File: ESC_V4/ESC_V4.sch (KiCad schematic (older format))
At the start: 43 parts

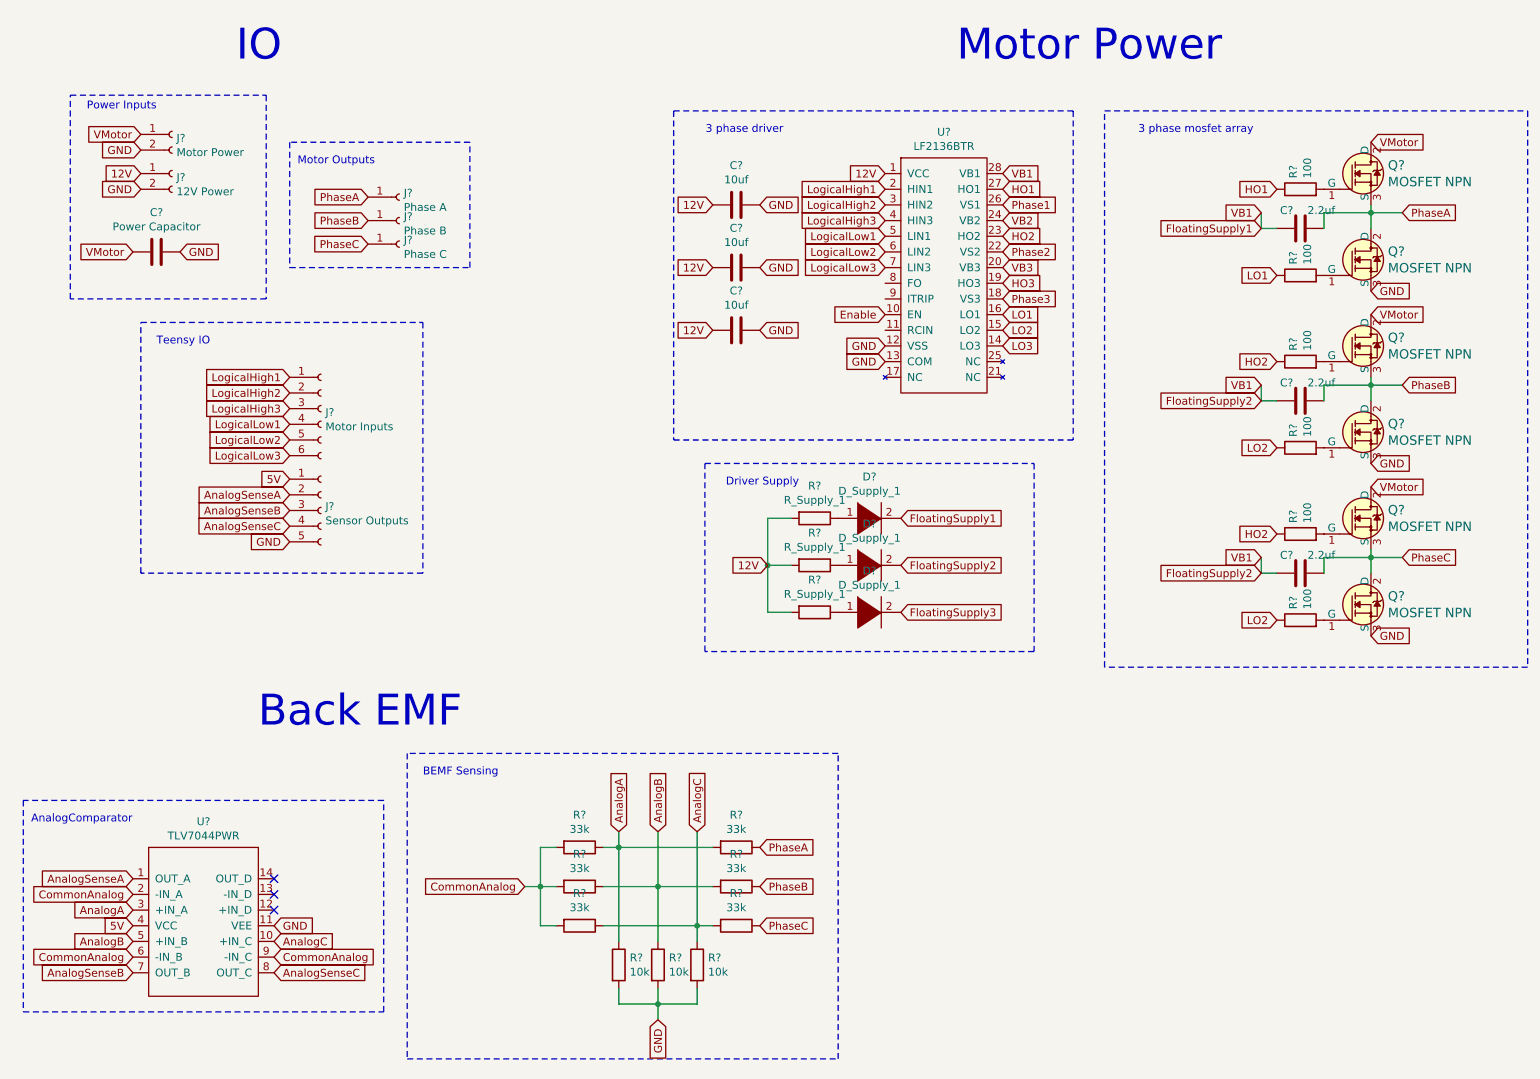
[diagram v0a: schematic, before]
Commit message: Footprint associations
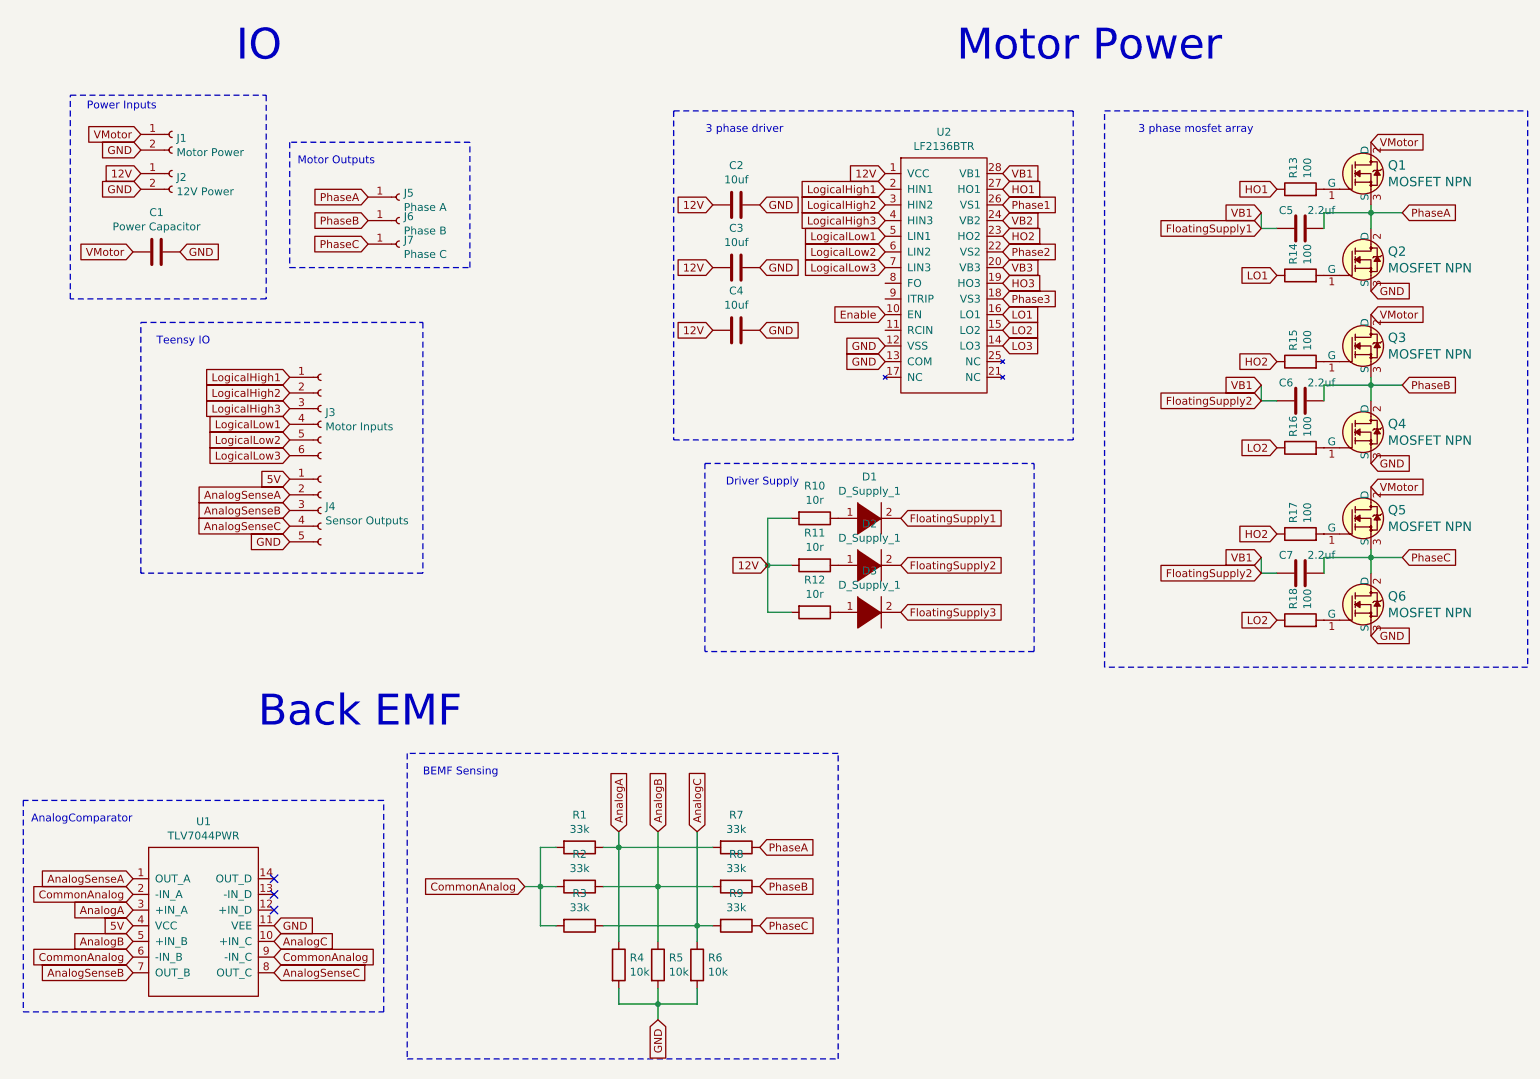
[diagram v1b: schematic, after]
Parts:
- C1: renamed from C?; footprint (none) -> Capacitor_SMD:C_Elec_10x10.2
- C2, C3, C4, C5, C6, C7: renamed from C?; footprint (none) -> Capacitor_SMD:C_0603_1608Metric
- D1, D2, D3: renamed from D?; footprint (none) -> Diode_SMD:D_SOD-323F
- J1: renamed from J?; footprint (none) -> XT60-M:AMASS_XT60-M
- J2: renamed from J?; footprint (none) -> Connector_PinHeader_2.54mm:PinHeader_1x02_P2.54mm_Vertical
- J3: renamed from J?; footprint (none) -> Connector_PinHeader_2.54mm:PinHeader_1x06_P2.54mm_Vertical
- J4: renamed from J?; footprint (none) -> Connector_PinHeader_2.54mm:PinHeader_1x05_P2.54mm_Vertical
- J5, J6, J7: renamed from J?; footprint (none) -> XT60-M:SquarePad4x4
- Q1, Q2, Q3, Q4, Q5: renamed from Q?; footprint digikey-footprints:TO-220-3 -> Package_TO_SOT_SMD:TO-252-2
- R1, R2, R3, R4: renamed from R?; footprint (none) -> Resistor_SMD:R_0603_1608Metric
- R10, R11, R12: renamed from R?; value R_Supply_1 -> 10r; footprint (none) -> Resistor_SMD:R_0201_0603Metric
- R13, R14, R15, R16, R17, R18, R5, R6, R7, R8, R9: renamed from R?; footprint (none) -> Resistor_SMD:R_0201_0603Metric
- U1: renamed from U?; footprint (none) -> Package_SO:TSSOP-14_4.4x5mm_P0.65mm
- U2: renamed from U?; footprint (none) -> Package_SO:SOIC-28W_7.5x17.9mm_P1.27mm
- gave numbers to parts that had none: 1

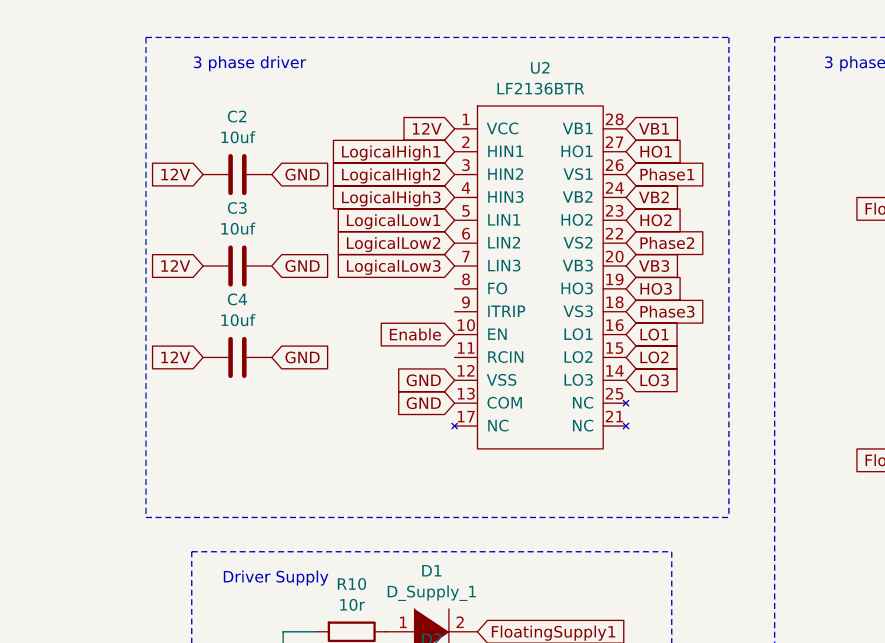
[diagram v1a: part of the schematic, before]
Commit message: Add components to driver and small tweaks
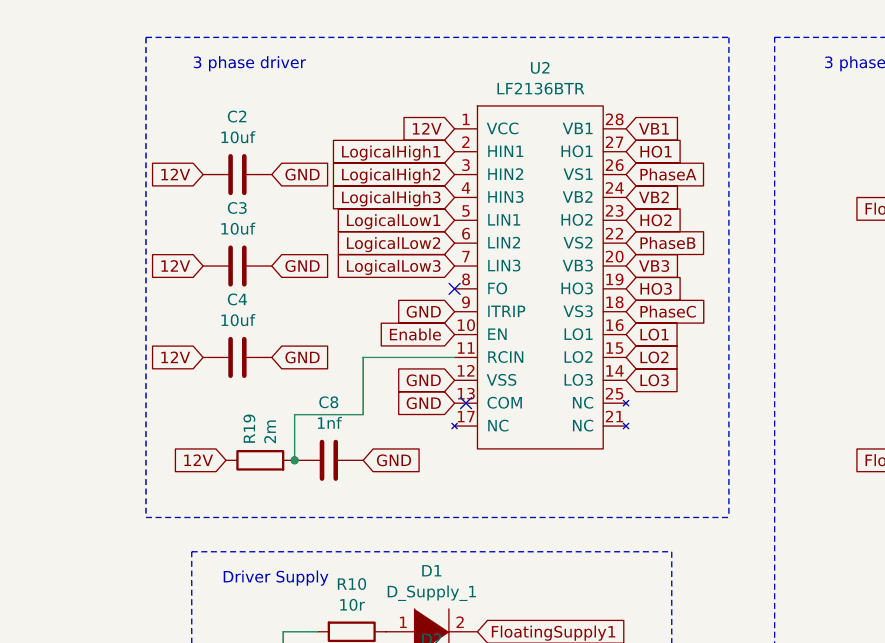
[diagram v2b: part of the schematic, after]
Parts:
- added C8: 1nf, Capacitor_SMD:C_0603_1608Metric, symbol Device:C
- added R19: 2m, Resistor_SMD:R_0201_0603Metric, symbol Device:R
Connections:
- net Phase1 is gone; now on net PhaseA: U2.26 (VS1)
- net Phase2 is gone; now on net PhaseB: U2.22 (VS2)
- net Phase3 is gone; now on net PhaseC: U2.18 (VS3)
- net 12V: now also R19.1
- net GND: now also U2.9 (ITRIP), C8.2
- net at U2.11 (RCIN): now also C8.1, R19.2
- no-connect marks 3 -> 5
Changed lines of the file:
@@
 LogicalLow3
 Text GLabel 7400 1900 2    50   Input ~ 0
-Phase1
+PhaseA
 Text GLabel 7400 2200 2    50   Input ~ 0
-Phase2
+PhaseB
 Text GLabel 7400 2500 2    50   Input ~ 0
-Phase3
+PhaseC
 Text GLabel 7400 1700 2    50   Input ~ 0
 VB1
@@
 	0    1    1    0
 $EndComp
+Text GLabel 6650 2500 0    50   Input ~ 0
+GND
+NoConn ~ 6650 2400
+NoConn ~ 6700 2900
+Wire Wire Line
+	6650 2700 6250 2700
+Wire Wire Line
+	5950 2950 5950 3150
+$Comp
+L Device:R R19
+U 1 1 623C84D3
+P 5800 3150
+F 0 "R19" H 5870 3196 50  0000 L CNN
+F 1 "2m" H 5870 3105 50  0000 L CNN
+F 2 "Resistor_SMD:R_0201_0603Metric" V 5730 3150 50  0001 C CNN
+F 3 "~" H 5800 3150 50  0001 C CNN
+	1    5800 3150
+	0    -1   -1   0
+$EndComp
+$Comp
+L Device:C C8
+U 1 1 623C9190
+P 6100 3150
+F 0 "C8" V 6352 3150 50  0000 C CNN
+F 1 "1nf" V 6261 3150 50  0000 C CNN
+F 2 "Capacitor_SMD:C_0603_1608Metric" H 6138 3000 50  0001 C CNN
+F 3 "~" H 6100 3150 50  0001 C CNN
+	1    6100 3150
+	0    -1   -1   0
+$EndComp
+Connection ~ 5950 3150
+Text GLabel 5650 3150 0    50   Input ~ 0
+12V
+Text GLabel 6250 3150 2    50   Input ~ 0
+GND
+Wire Wire Line
+	5950 2950 6250 2950
+Wire Wire Line
+	6250 2950 6250 2700
 $EndSCHEMATC

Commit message: Start of pcb layout
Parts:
- Q6: footprint digikey-footprints:TO-220-3 -> Package_TO_SOT_SMD:TO-252-2
- R10, R11, R12, R13, R14, R15, R16, R17, R18, R19, R5, R6, R7, R8, R9: footprint Resistor_SMD:R_0201_0603Metric -> Resistor_SMD:R_0603_1608Metric
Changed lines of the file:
@@
 F 0 "R7" V 5493 6000 50  0000 C CNN
 F 1 "33k" V 5584 6000 50  0000 C CNN
-F 2 "Resistor_SMD:R_0201_0603Metric" V 5630 6000 50  0001 C CNN
+F 2 "Resistor_SMD:R_0603_1608Metric" V 5630 6000 50  0001 C CNN
 F 3 "~" H 5700 6000 50  0001 C CNN
 	1    5700 6000
@@
 F 0 "R8" V 5493 6250 50  0000 C CNN
 F 1 "33k" V 5584 6250 50  0000 C CNN
-F 2 "Resistor_SMD:R_0201_0603Metric" V 5630 6250 50  0001 C CNN
+F 2 "Resistor_SMD:R_0603_1608Metric" V 5630 6250 50  0001 C CNN
 F 3 "~" H 5700 6250 50  0001 C CNN
 	1    5700 6250
@@
 F 0 "R9" V 5493 6500 50  0000 C CNN
 F 1 "33k" V 5584 6500 50  0000 C CNN
-F 2 "Resistor_SMD:R_0201_0603Metric" V 5630 6500 50  0001 C CNN
+F 2 "Resistor_SMD:R_0603_1608Metric" V 5630 6500 50  0001 C CNN
 F 3 "~" H 5700 6500 50  0001 C CNN
 	1    5700 6500
@@
 F 0 "R5" H 5270 6796 50  0000 L CNN
 F 1 "10k" H 5270 6705 50  0000 L CNN
-F 2 "Resistor_SMD:R_0201_0603Metric" V 5130 6750 50  0001 C CNN
+F 2 "Resistor_SMD:R_0603_1608Metric" V 5130 6750 50  0001 C CNN
 F 3 "~" H 5200 6750 50  0001 C CNN
 	1    5200 6750
@@
 F 0 "R6" H 5520 6796 50  0000 L CNN
 F 1 "10k" H 5520 6705 50  0000 L CNN
-F 2 "Resistor_SMD:R_0201_0603Metric" V 5380 6750 50  0001 C CNN
+F 2 "Resistor_SMD:R_0603_1608Metric" V 5380 6750 50  0001 C CNN
 F 3 "~" H 5450 6750 50  0001 C CNN
 	1    5450 6750
@@
 F 0 "Q6" H 9858 4503 60  0000 L CNN
 F 1 "MOSFET NPN" H 9858 4397 60  0000 L CNN
-F 2 "digikey-footprints:TO-220-3" H 9950 4650 60  0001 L CNN
+F 2 "Package_TO_SOT_SMD:TO-252-2" H 9950 4650 60  0001 L CNN
 F 3 "https://www.infineon.com/dgdl/irlb8721pbf.pdf?fileId=5546d462533600a40153566056732591" H 9950 4750 60  0001 L CNN
 F 4 "IRLB8721PBF-ND" H 9950 4850 60  0001 L CNN "Digi-Key_PN"
@@
 F 0 "R18" H 9370 4596 50  0000 L CNN
 F 1 "100" H 9370 4505 50  0000 L CNN
-F 2 "Resistor_SMD:R_0201_0603Metric" V 9230 4550 50  0001 C CNN
+F 2 "Resistor_SMD:R_0603_1608Metric" V 9230 4550 50  0001 C CNN
 F 3 "~" H 9300 4550 50  0001 C CNN
 	1    9300 4550
@@
 F 0 "R17" H 9370 4046 50  0000 L CNN
 F 1 "100" H 9370 3955 50  0000 L CNN
-F 2 "Resistor_SMD:R_0201_0603Metric" V 9230 4000 50  0001 C CNN
+F 2 "Resistor_SMD:R_0603_1608Metric" V 9230 4000 50  0001 C CNN
 F 3 "~" H 9300 4000 50  0001 C CNN
 	1    9300 4000
@@
 F 0 "R16" H 9370 3496 50  0000 L CNN
 F 1 "100" H 9370 3405 50  0000 L CNN
-F 2 "Resistor_SMD:R_0201_0603Metric" V 9230 3450 50  0001 C CNN
+F 2 "Resistor_SMD:R_0603_1608Metric" V 9230 3450 50  0001 C CNN
 F 3 "~" H 9300 3450 50  0001 C CNN
 	1    9300 3450
@@
 F 0 "R15" H 9370 2946 50  0000 L CNN
 F 1 "100" H 9370 2855 50  0000 L CNN
-F 2 "Resistor_SMD:R_0201_0603Metric" V 9230 2900 50  0001 C CNN
+F 2 "Resistor_SMD:R_0603_1608Metric" V 9230 2900 50  0001 C CNN
 F 3 "~" H 9300 2900 50  0001 C CNN
 	1    9300 2900
@@
 F 0 "R14" H 9370 2396 50  0000 L CNN
 F 1 "100" H 9370 2305 50  0000 L CNN
-F 2 "Resistor_SMD:R_0201_0603Metric" V 9230 2350 50  0001 C CNN
+F 2 "Resistor_SMD:R_0603_1608Metric" V 9230 2350 50  0001 C CNN
 F 3 "~" H 9300 2350 50  0001 C CNN
 	1    9300 2350
@@
 F 0 "R13" H 9370 1846 50  0000 L CNN
 F 1 "100" H 9370 1755 50  0000 L CNN
-F 2 "Resistor_SMD:R_0201_0603Metric" V 9230 1800 50  0001 C CNN
+F 2 "Resistor_SMD:R_0603_1608Metric" V 9230 1800 50  0001 C CNN
 F 3 "~" H 9300 1800 50  0001 C CNN
 	1    9300 1800
@@
 F 0 "R12" V 5993 4500 50  0000 C CNN
 F 1 "10r" V 6084 4500 50  0000 C CNN
-F 2 "Resistor_SMD:R_0201_0603Metric" V 6130 4500 50  0001 C CNN
+F 2 "Resistor_SMD:R_0603_1608Metric" V 6130 4500 50  0001 C CNN
 F 3 "~" H 6200 4500 50  0001 C CNN
 	1    6200 4500
@@
 F 0 "R11" V 5993 4200 50  0000 C CNN
 F 1 "10r" V 6084 4200 50  0000 C CNN
-F 2 "Resistor_SMD:R_0201_0603Metric" V 6130 4200 50  0001 C CNN
+F 2 "Resistor_SMD:R_0603_1608Metric" V 6130 4200 50  0001 C CNN
 F 3 "~" H 6200 4200 50  0001 C CNN
 	1    6200 4200
@@
 F 0 "R10" V 5993 3900 50  0000 C CNN
 F 1 "10r" V 6084 3900 50  0000 C CNN
-F 2 "Resistor_SMD:R_0201_0603Metric" V 6130 3900 50  0001 C CNN
+F 2 "Resistor_SMD:R_0603_1608Metric" V 6130 3900 50  0001 C CNN
 F 3 "~" H 6200 3900 50  0001 C CNN
 	1    6200 3900
@@
 F 0 "R19" H 5870 3196 50  0000 L CNN
 F 1 "2m" H 5870 3105 50  0000 L CNN
-F 2 "Resistor_SMD:R_0201_0603Metric" V 5730 3150 50  0001 C CNN
+F 2 "Resistor_SMD:R_0603_1608Metric" V 5730 3150 50  0001 C CNN
 F 3 "~" H 5800 3150 50  0001 C CNN
 	1    5800 3150

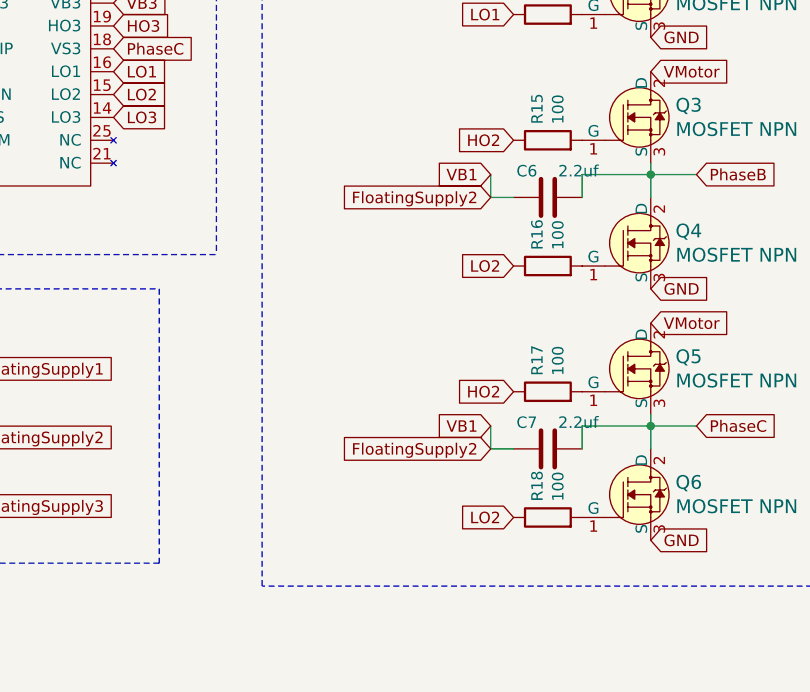
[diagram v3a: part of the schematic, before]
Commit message: Starting routing, not super happy about positions
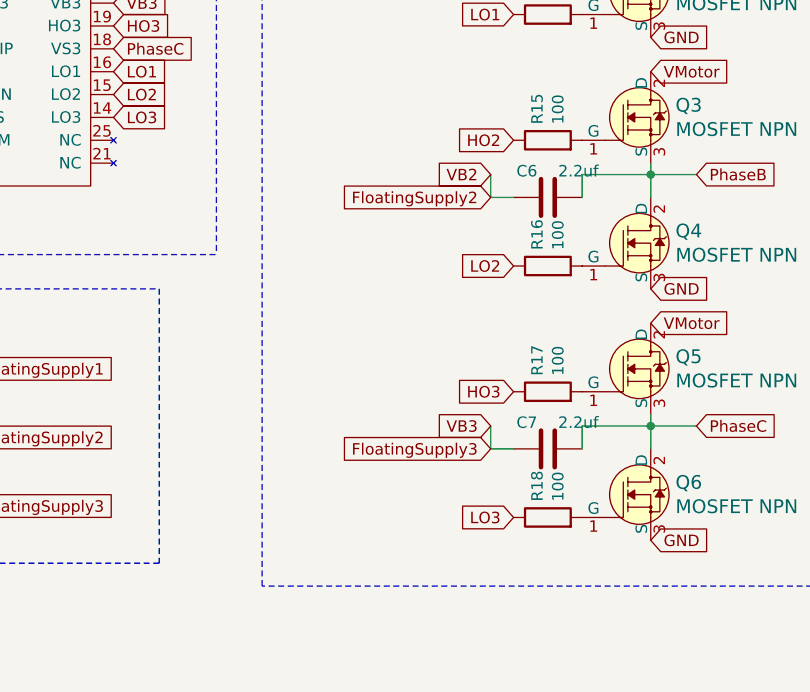
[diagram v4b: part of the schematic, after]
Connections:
- net VB3 is gone; now on net FloatingSupply3: U2.20 (VB3)
- net FloatingSupply1: no longer C6.1, C7.1, D2.2 (A)
- net FloatingSupply3: now also C7.1
- net HO2: no longer R17.1
- net HO3: now also R17.1
- net LO2: no longer R18.1
- net LO3: now also R18.1
- net VB2 renamed FloatingSupply2
- net FloatingSupply2: now also C6.1, D2.2 (A)
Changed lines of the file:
@@
 	8050 1300 10750 1300
 Text GLabel 9150 4550 0    50   Input ~ 0
-LO2
+LO3
 Text GLabel 9150 4000 0    50   Input ~ 0
-HO2
+HO3
 Wire Wire Line
 	9050 4250 9150 4250
@@
 	9050 4150 9050 4250
 Text GLabel 9050 4250 0    50   Input ~ 0
-FloatingSupply2
+FloatingSupply3
 Text GLabel 9050 4150 0    50   Input ~ 0
-VB1
+VB3
 Text GLabel 9150 3450 0    50   Input ~ 0
 LO2
@@
 FloatingSupply2
 Text GLabel 9050 3050 0    50   Input ~ 0
-VB1
+VB2
 Text GLabel 9150 2350 0    50   Input ~ 0
 LO1

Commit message: Potentially finished layout
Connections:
- net Enable is gone; now on net 5V: U2.10 (EN)
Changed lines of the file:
@@
 AnalogComparator
 Text GLabel 6650 2600 0    50   Input ~ 0
-Enable
+5V
 $Comp
 L Connector:Conn_01x06_Female J3
